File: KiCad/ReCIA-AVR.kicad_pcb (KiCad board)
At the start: 4 copper layers, 17.4 x 51.4 mm, 6 parts, among them U1 AVR128DA64-I_MR, U5 8520_DIP

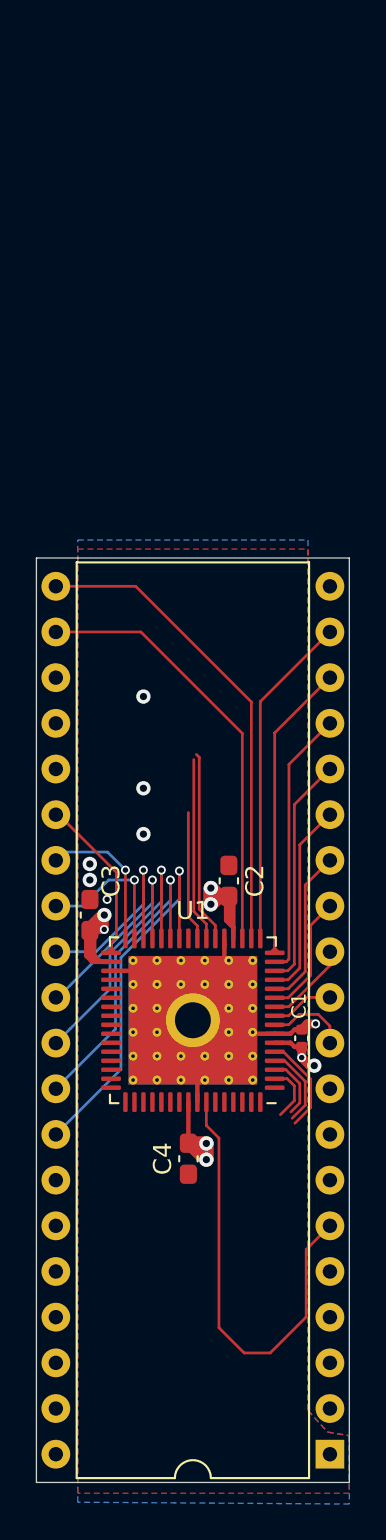
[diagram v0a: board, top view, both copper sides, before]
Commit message: Pin assignment of A0-A3, SP, CNT signals for the AVR-version and more routing done
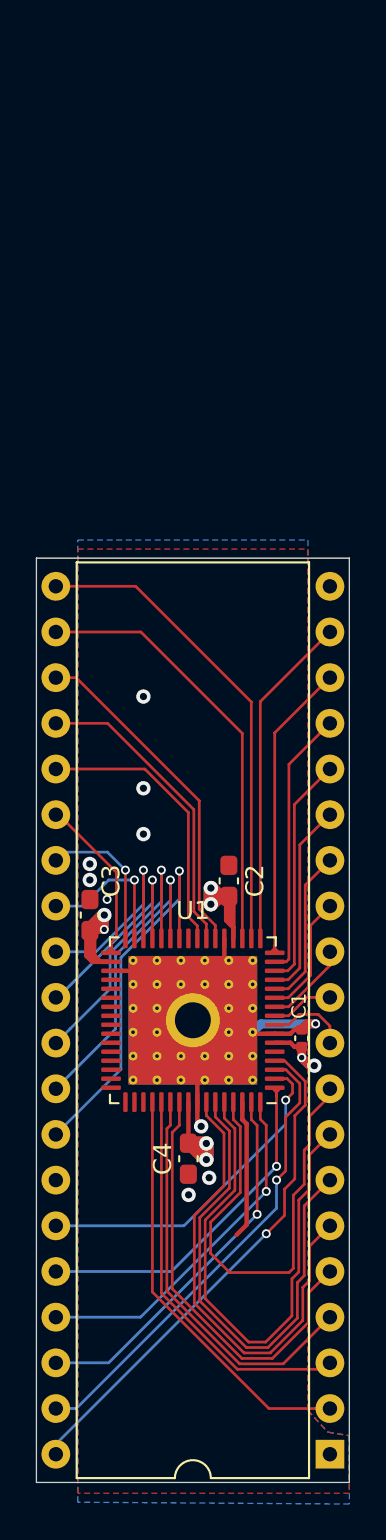
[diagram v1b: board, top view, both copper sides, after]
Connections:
- U1 pad 1: Net-(U1-Pad1) -> A2
- U1 pad 2: A0 -> A3
- U1 pad 3: A1 -> SP
- U1 pad 4: A2 -> CNT
- U1 pad 5: A3 -> Net-(U1-Pad5)
- U1 pad 63: Net-(U1-Pad63) -> A0
- U1 pad 64: Net-(U1-Pad64) -> A1
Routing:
- net PA6: track 0.00 -> 29.2 mm
- net CNT: track 0.00 -> 28.6 mm, vias 0 -> 1
- net PA5: track 0.00 -> 27.7 mm
- net SP: track 0.00 -> 26.1 mm, vias 0 -> 1
- net PA7: track 0.00 -> 25.2 mm
- net PA3: track 0.00 -> 23.9 mm
- net PA0: track 0.00 -> 23.1 mm
- net PA2: track 0.00 -> 22.4 mm
- net PA1: track 0.00 -> 21.9 mm
- net A0: track 3.18 -> 21.0 mm, vias 0 -> 1
- net A2: track 4.53 -> 20.9 mm, vias 0 -> 1
- net A1: track 3.50 -> 19.7 mm, vias 0 -> 1
- net A3: track 5.45 -> 18.6 mm, vias 0 -> 1
- net E-CLK: track 7.21 -> 15.6 mm
- net CS: track 10.7 -> 18.8 mm
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
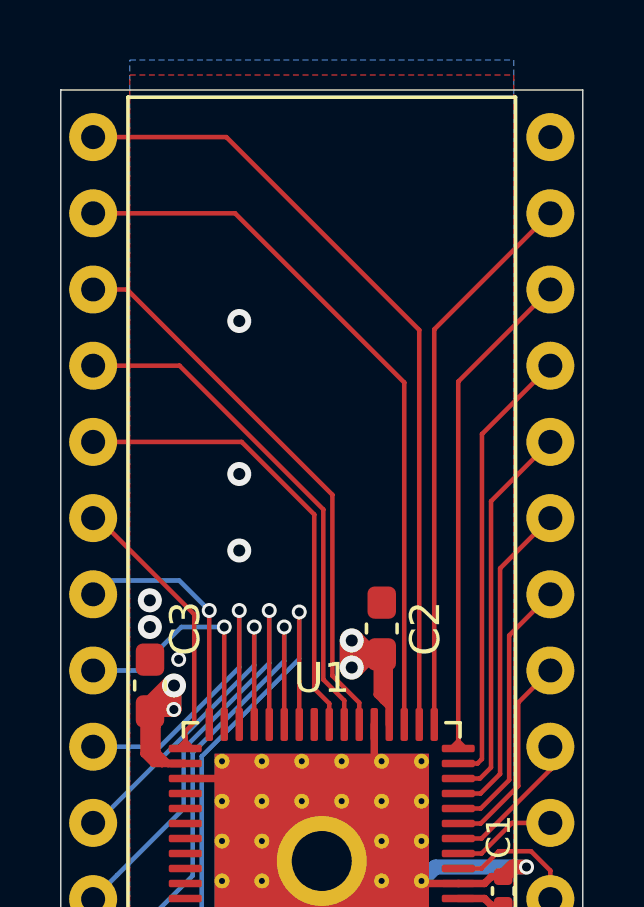
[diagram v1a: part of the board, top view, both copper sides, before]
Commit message: Add a 74AHCT1G17 - Single Schmitt trigger buffer for the E-CLK on the AVR version
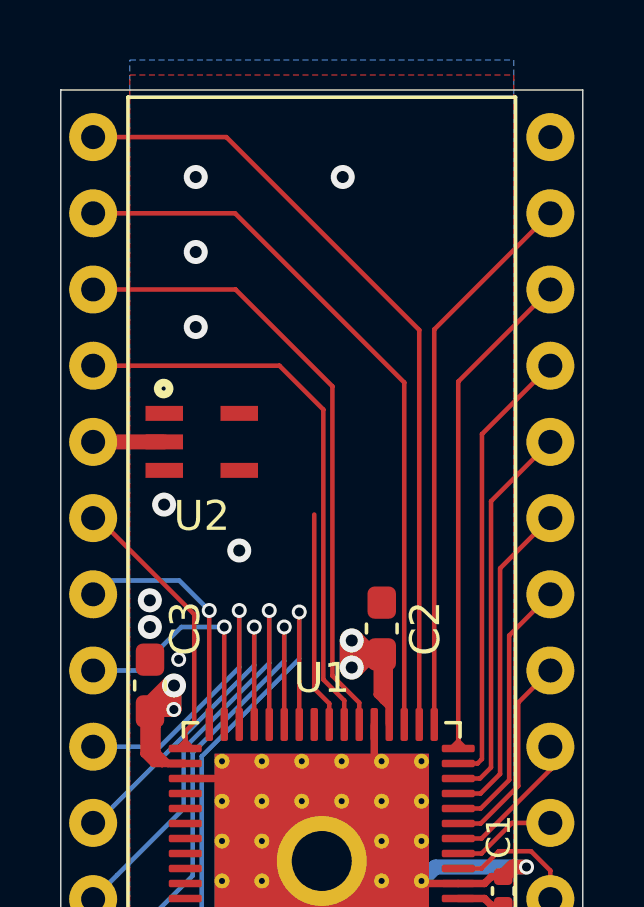
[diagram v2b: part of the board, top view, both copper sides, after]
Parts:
- added U2: 74AHCT1G17, ReCIA:SOT95P275X110-5N, F.Cu at (128.0, 69.0)
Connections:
- U5 pad 25: E-CLK -> E
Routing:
- net E-CLK: track 15.6 -> 7.21 mm
- net E: track 0.00 -> 2.37 mm
- net CS: track 18.8 -> 21.0 mm
- net FLAG: track 17.1 -> 19.1 mm
- net GND: vias 10 -> 13
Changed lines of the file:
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@@
     (thickness 1.6)
     (drawings 4)
-    (tracks 342)
+    (tracks 344)
     (zones 0)
-    (modules 6)
-    (nets 59)
+    (modules 7)
+    (nets 61)
   )
   (page A4)
@@
   )
   (setup
-    (last_trace_width 0.5)
+    (last_trace_width 0.1524)
     (user_trace_width 0.2)
     (user_trace_width 0.25)
@@
   (net 57 XTAL32K1)
   (net 58 "Net-(U1-Pad5)")
+  (net 59 "Net-(U2-Pad1)")
+  (net 60 E)
   (net_class Default "This is the default net class."
     (clearance 0.15)
@@
     (add_net D6)
     (add_net D7)
+    (add_net E)
     (add_net E-CLK)
     (add_net EXTCLK)
@@
     (add_net "Net-(U1-Pad49)")
     (add_net "Net-(U1-Pad5)")
+    (add_net "Net-(U2-Pad1)")
     (add_net PA0)
     (add_net PA1)
@@
     (add_net XTAL32K1)
     (add_net XTAL32K2)
+  )
+  (module ReCIA:SOT95P275X110-5N (layer F.Cu)
+    (at 128 69.03)
+    (descr SOT753)
+    (tags "Integrated Circuit")
+    (attr smd)
+    (fp_text reference U2 (at 0 2.47) (layer F.SilkS)
+      (effects (font (size 1 1) (thickness 0.15)))
+    )
+    (fp_text value 74AHCT1G17 (at 0 0) (layer F.SilkS) hide
+      (effects (font (size 1.27 1.27) (thickness 0.254)))
+    )
+    (fp_text user %R (at 0 0) (layer F.Fab) hide
+      (effects (font (size 1.27 1.27) (thickness 0.254)))
+    )
+    (fp_circle (center -1.27 -1.778) (end -1.143 -1.778) (layer F.SilkS) (width 0.4))
+    (fp_line (start -0.75 -0.5) (end 0.2 -1.45) (layer F.Fab) (width 0.1))
+    (fp_line (start -0.75 1.45) (end -0.75 -1.45) (layer F.Fab) (width 0.1))
+    (fp_line (start 0.75 1.45) (end -0.75 1.45) (layer F.Fab) (width 0.1))
+    (fp_line (start 0.75 -1.45) (end 0.75 1.45) (layer F.Fab) (width 0.1))
+    (fp_line (start -0.75 -1.45) (end 0.75 -1.45) (layer F.Fab) (width 0.1))
+    (fp_line (start -2.125 1.8) (end -2.125 -1.8) (layer F.CrtYd) (width 0.05))
+    (fp_line (start 2.125 1.8) (end -2.125 1.8) (layer F.CrtYd) (width 0.05))
+    (fp_line (start 2.125 -1.8) (end 2.125 1.8) (layer F.CrtYd) (width 0.05))
+    (fp_line (start -2.125 -1.8) (end 2.125 -1.8) (layer F.CrtYd) (width 0.05))
+    (pad 5 smd rect (at 1.25 -0.95 90) (size 0.5 1.25) (layers F.Cu F.Paste F.Mask)
+      (net 1 VCC))
+    (pad 4 smd rect (at 1.25 0.95 90) (size 0.5 1.25) (layers F.Cu F.Paste F.Mask)
+      (net 28 E-CLK))
+    (pad 3 smd rect (at -1.25 0.95 90) (size 0.5 1.25) (layers F.Cu F.Paste F.Mask)
+      (net 2 GND))
+    (pad 2 smd rect (at -1.25 0 90) (size 0.5 1.25) (layers F.Cu F.Paste F.Mask)
+      (net 60 E))
+    (pad 1 smd rect (at -1.25 -0.95 90) (size 0.5 1.25) (layers F.Cu F.Paste F.Mask)
+      (net 59 "Net-(U2-Pad1)"))
+    (model ${KISYS3DMOD}/Package_SO.3dshapes/TSOP-5_1.65x3.05mm_P0.95mm.wrl
+      (at (xyz 0 0 0))
+      (scale (xyz 1 1 1))
+      (rotate (xyz 0 0 0))
+    )
   )
   (module Capacitor_SMD:C_0402_1005Metric (layer F.Cu)
@@
       (net 27 PA4))
     (pad 25 thru_hole oval (at 7.62 13.97 180) (size 1.6 1.6) (drill 0.8) (layers *.Cu *.Mask)
-      (net 28 E-CLK))
+      (net 60 E))
     (pad 5 thru_hole oval (at -7.62 -13.97 180) (size 1.6 1.6) (drill 0.8) (layers *.Cu *.Mask)
       (net 29 PA3))
@@
   (via (at 132.461 88.9) (size 0.8) (drill 0.4) (layers F.Cu B.Cu) (net 2))
   (via (at 138.825 83.2) (size 0.5) (drill 0.3) (layers F.Cu B.Cu) (net 2))
-  (via (at 129.25 65) (size 0.8) (drill 0.4) (layers F.Cu B.Cu) (net 2))
-  (via (at 129.25 70.1) (size 0.8) (drill 0.4) (layers F.Cu B.Cu) (net 2))
+  (via (at 127.8 65.2) (size 0.8) (drill 0.4) (layers F.Cu B.Cu) (net 2))
+  (via (at 126.746 71.12) (size 0.8) (drill 0.4) (layers F.Cu B.Cu) (net 2))
   (via (at 129.25 72.65) (size 0.8) (drill 0.4) (layers F.Cu B.Cu) (net 2))
   (segment (start 133.75 81.25) (end 132 83) (width 0.25) (layer F.Cu) (net 2))
@@
   (segment (start 135.79 83.2) (end 135.325 83.665) (width 0.5) (layer B.Cu) (net 2))
   (segment (start 138.825 83.2) (end 135.79 83.2) (width 0.5) (layer B.Cu) (net 2))
+  (via (at 127.8 62.7) (size 0.8) (drill 0.4) (layers F.Cu B.Cu) (net 2))
+  (via (at 127.8 60.2) (size 0.8) (drill 0.4) (layers F.Cu B.Cu) (net 2))
+  (via (at 132.7 60.2) (size 0.8) (drill 0.4) (layers F.Cu B.Cu) (net 2))
   (segment (start 135.25 87.55) (end 135.25 88.514) (width 0.1524) (layer F.Cu) (net 3))
   (segment (start 135.255 88.528615) (end 135.5725 88.846115) (width 0.1524) (layer F.Cu) (net 3))
@@
   (segment (start 129.09 99.51) (end 136.0805 92.5195) (width 0.1524) (layer B.Cu) (net 4))
   (segment (start 124.38 99.51) (end 129.09 99.51) (width 0.1524) (layer B.Cu) (net 4))
-  (via (at 136.0805 94.869) (size 0.5) (drill 0.3) (layers F.Cu B.Cu) (net 33))
   (segment (start 136.55 79.75) (end 137.19036 79.75) (width 0.1524) (layer F.Cu) (net 5))
   (segment (start 137.19036 79.75) (end 137.34036 79.6) (width 0.1524) (layer F.Cu) (net 5))
@@
   (segment (start 132.25 77.75) (end 131.75 77.25) (width 0.1524) (layer F.Cu) (net 28))
   (segment (start 132.25 78.45) (end 132.25 77.75) (width 0.1524) (layer F.Cu) (net 28))
-  (segment (start 129.33 69.03) (end 131.75 71.45) (width 0.1524) (layer F.Cu) (net 28))
-  (segment (start 124.38 69.03) (end 129.33 69.03) (width 0.1524) (layer F.Cu) (net 28))
   (segment (start 138.414909 99.812763) (end 138.41491 98.17509) (width 0.1524) (layer F.Cu) (net 29))
   (segment (start 131.25 88.841001) (end 130.854822 89.236179) (width 0.1524) (layer F.Cu) (net 29))
@@
   (segment (start 136.229312 104.59) (end 129.75 98.110688) (width 0.1524) (layer F.Cu) (net 32))
   (segment (start 139.62 104.59) (end 136.229312 104.59) (width 0.1524) (layer F.Cu) (net 32))
-  (via (at 136.652 91.8845) (size 0.5) (drill 0.3) (layers F.Cu B.Cu) (net 34))
+  (via (at 136.0805 94.869) (size 0.5) (drill 0.3) (layers F.Cu B.Cu) (net 33))
   (segment (start 124.38 106.5695) (end 136.0805 94.869) (width 0.1524) (layer B.Cu) (net 33))
   (segment (start 124.38 107.13) (end 124.38 106.5695) (width 0.1524) (layer B.Cu) (net 33))
@@
   (segment (start 137.0965 92.3925) (end 137.668 91.821) (width 0.1524) (layer F.Cu) (net 33))
   (segment (start 136.0805 94.869) (end 137.0965 93.853) (width 0.1524) (layer F.Cu) (net 33))
+  (via (at 136.652 91.8845) (size 0.5) (drill 0.3) (layers F.Cu B.Cu) (net 34))
   (segment (start 137.172328 85.75) (end 136.55 85.75) (width 0.1524) (layer F.Cu) (net 34))
   (segment (start 136.652 91.8845) (end 137.16 91.3765) (width 0.1524) (layer F.Cu) (net 34))
@@
   (segment (start 136.55 79) (end 136.32379 79.22621) (width 0.1524) (layer F.Cu) (net 36))
   (segment (start 136.55 79) (end 136.8 79.25) (width 0.1524) (layer F.Cu) (net 36))
+  (segment (start 130.59 66.49) (end 124.38 66.49) (width 0.1524) (layer F.Cu) (net 37))
+  (segment (start 132.05241 67.95241) (end 130.59 66.49) (width 0.1524) (layer F.Cu) (net 37))
+  (segment (start 132.05241 76.95241) (end 132.05241 67.95241) (width 0.1524) (layer F.Cu) (net 37))
+  (segment (start 132.75 77.65) (end 132.05241 76.95241) (width 0.1524) (layer F.Cu) (net 37))
   (segment (start 132.75 78.45) (end 132.75 77.65) (width 0.1524) (layer F.Cu) (net 37))
-  (segment (start 132.75 77.65) (end 132.05241 76.95241) (width 0.1524) (layer F.Cu) (net 37))
-  (segment (start 132.05241 71.28291) (end 132.05241 76.95241) (width 0.1524) (layer F.Cu) (net 37))
-  (segment (start 127.2595 66.49) (end 132.05241 71.28291) (width 0.1524) (layer F.Cu) (net 37))
-  (segment (start 124.38 66.49) (end 127.2595 66.49) (width 0.1524) (layer F.Cu) (net 37))
-  (segment (start 133.25 78.45) (end 133.25 77.722328) (width 0.1524) (layer F.Cu) (net 38))
-  (segment (start 133.25 77.722328) (end 132.35482 76.827148) (width 0.1524) (layer F.Cu) (net 38))
-  (segment (start 132.35482 70.79345) (end 132.35482 76.827148) (width 0.1524) (layer F.Cu) (net 38))
-  (segment (start 125.51137 63.95) (end 132.35482 70.79345) (width 0.1524) (layer F.Cu) (net 38))
-  (segment (start 124.38 63.95) (end 125.51137 63.95) (width 0.1524) (layer F.Cu) (net 38))
+  (segment (start 133.25 77.722328) (end 133.25 78.45) (width 0.1524) (layer F.Cu) (net 38))
+  (segment (start 132.35482 67.178042) (end 132.35482 76.827148) (width 0.1524) (layer F.Cu) (net 38))
+  (segment (start 129.126778 63.95) (end 132.35482 67.178042) (width 0.1524) (layer F.Cu) (net 38))
+  (segment (start 132.35482 76.827148) (end 133.25 77.722328) (width 0.1524) (layer F.Cu) (net 38))
+  (segment (start 124.38 63.95) (end 129.126778 63.95) (width 0.1524) (layer F.Cu) (net 38))
   (segment (start 134.75 78.45) (end 134.75 67.05) (width 0.1524) (layer F.Cu) (net 39))
   (segment (start 129.11 61.41) (end 124.38 61.41) (width 0.1524) (layer F.Cu) (net 39))
@@
   (segment (start 134.75 87.55) (end 134.75 88.5203) (width 0.25) (layer F.Cu) (net 50))
   (segment (start 134.989436 94.372564) (end 134.4295 94.9325) (width 0.25) (layer F.Cu) (net 50))
+  (segment (start 126.75 69.03) (end 124.38 69.03) (width 0.5) (layer F.Cu) (net 60))
   (zone (net 2) (net_name GND) (layer F.Cu) (hatch edge 0.508)
     (connect_pads (clearance 0.15))

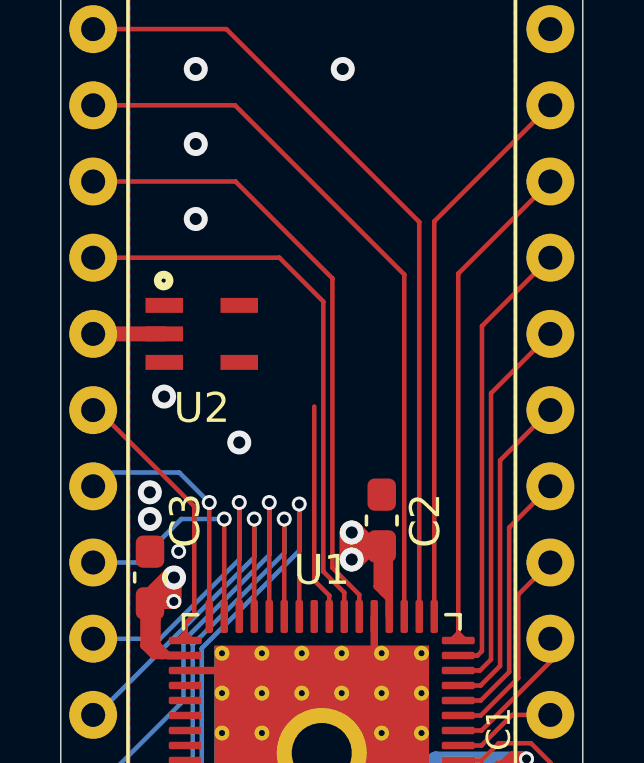
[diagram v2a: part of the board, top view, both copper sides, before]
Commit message: Add decoupling cap for 74AHCT1G17 on the AVR version
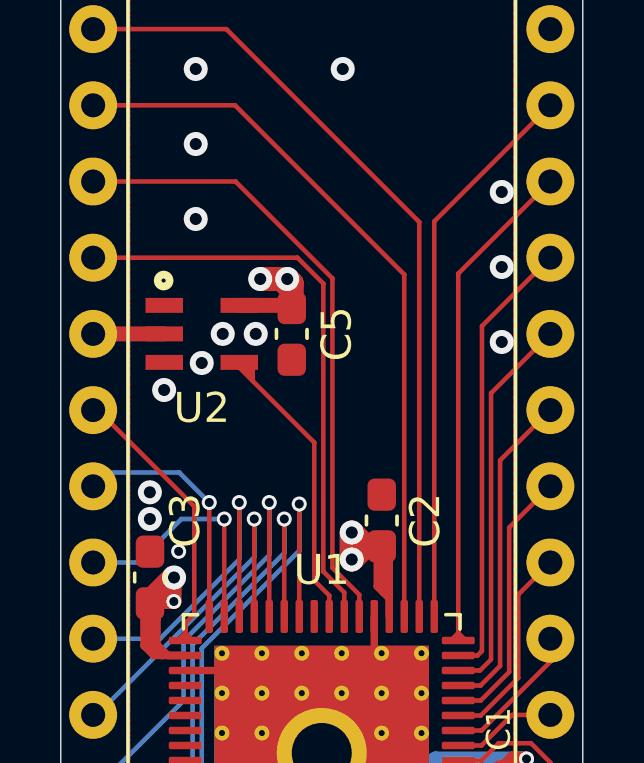
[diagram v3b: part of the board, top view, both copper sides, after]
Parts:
- added C5: 0.1uF, Capacitor_SMD:C_0603_1608Metric_Pad1.08x0.95mm_HandSolder, F.Cu at (131.0, 69.0)
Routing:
- net VCC: track 34.1 -> 39.1 mm, vias 8 -> 10
- net E-CLK: track 7.21 -> 11.9 mm
- net GND: vias 13 -> 18

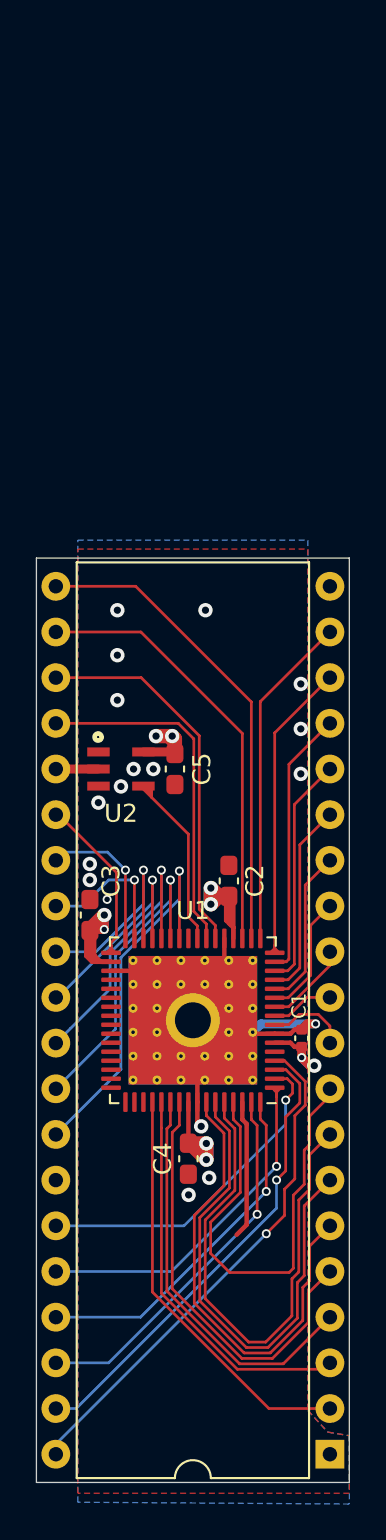
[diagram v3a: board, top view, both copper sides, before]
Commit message: Add a 33 Ohm damping resistor on the E-CLK buffer out line
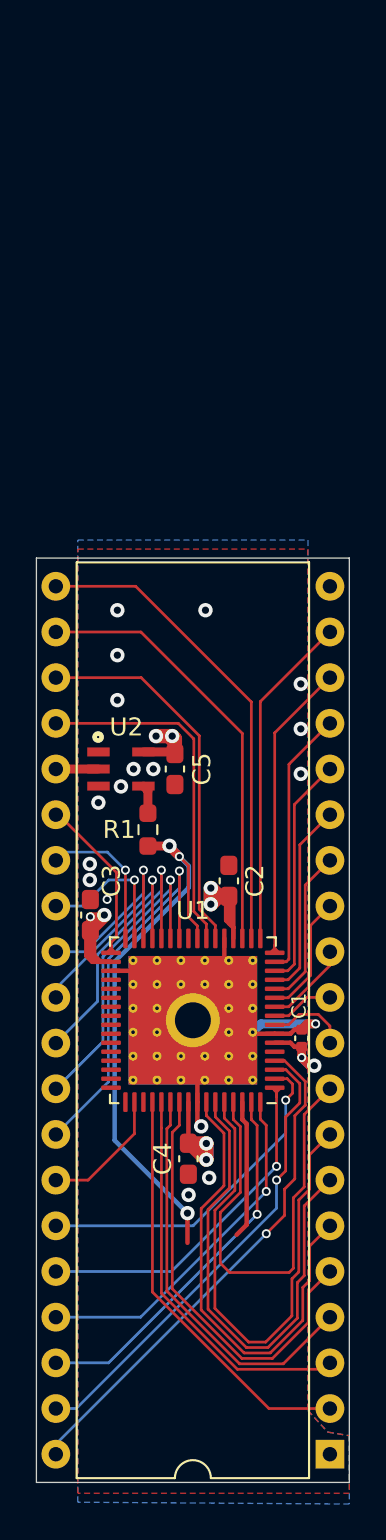
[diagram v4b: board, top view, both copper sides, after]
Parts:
- added R1: 33, Resistor_SMD:R_0603_1608Metric_Pad0.98x0.95mm_HandSolder, F.Cu at (129.5, 72.4)
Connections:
- U2 pad 4: E-CLK -> /ECLK
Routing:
- net E-CLK: track 11.9 -> 34.9 mm, vias 0 -> 3
- net RESET: track 0.00 -> 7.20 mm
- net /ECLK: track 0.00 -> 1.61 mm
- net VCC: track 39.1 -> 38.4 mm
